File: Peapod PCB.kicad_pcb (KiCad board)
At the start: 2 copper layers, 70.9 x 27.2 mm, 20 parts, among them U1 ESP8266

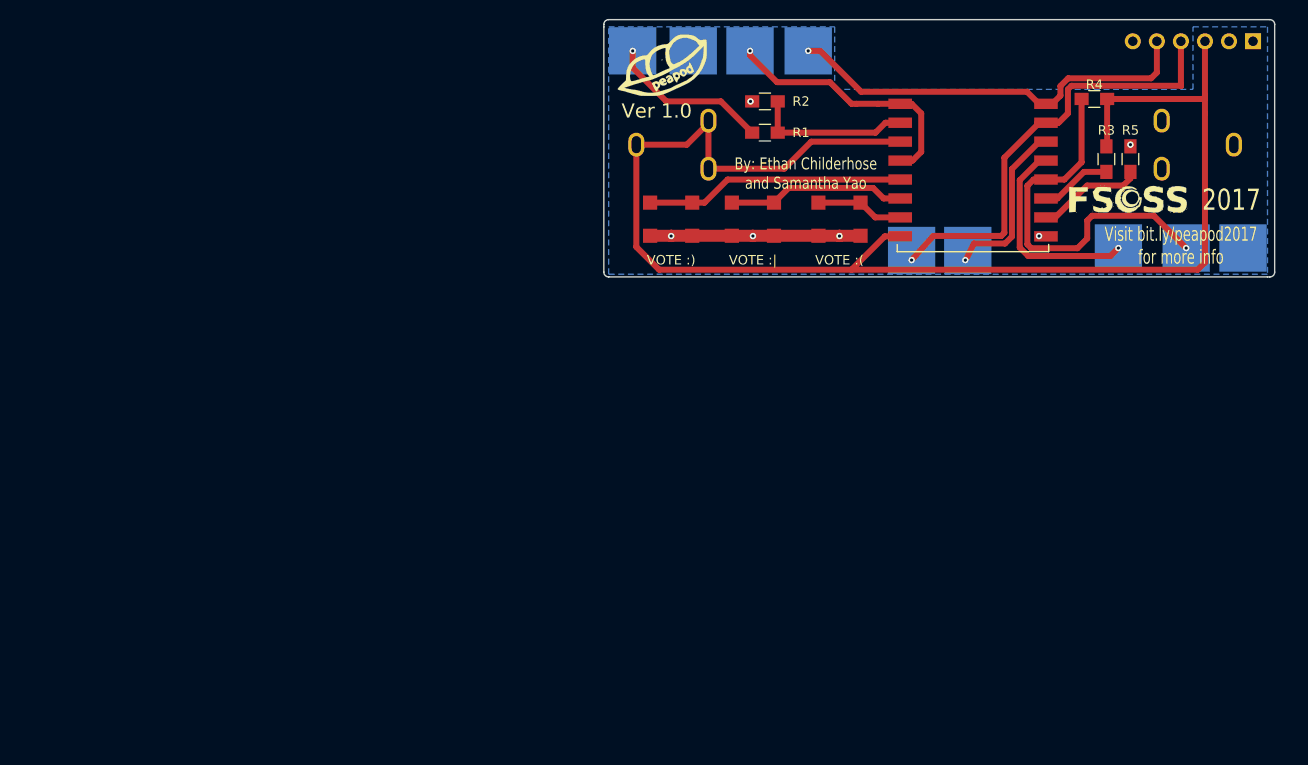
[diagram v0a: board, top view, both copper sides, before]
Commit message: initial plan for the outline of new peapod
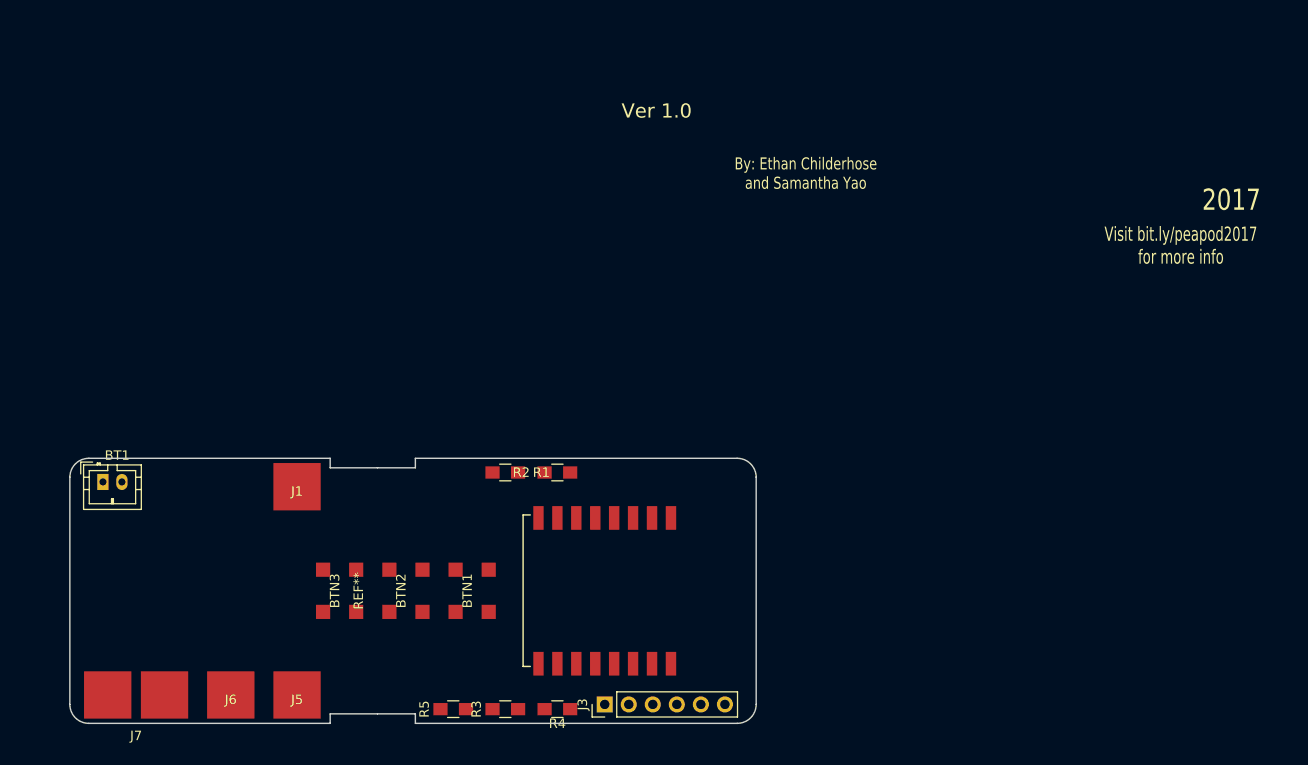
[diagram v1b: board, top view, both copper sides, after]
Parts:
- removed ANALOG, GPIO4, GPIO5, RX, TX: CONN_01X01, mod:Alligator Pad
- removed FTDI 3.3V: CONN_01X06, Pin_Headers:Pin_Header_Straight_1x06_Pitch2.54mm
- removed G***: LOGO, mod:LOGO
- removed G***: LOGO, mod:fsoss
- removed GND   GPIO0: CONN_01X02, mod:Bridge Pad
- removed RESET   GND: CONN_01X02, mod:Bridge Pad
- removed VOTE :(: Pushbutton, mod:Pushbutton
- removed VOTE :): Pushbutton, mod:Pushbutton
- removed VOTE :|: Pushbutton, mod:Pushbutton
- added BTN1: Pushbutton, mod:Pushbutton, F.Cu at (139.0, 86.5)
- added BTN2: Pushbutton, mod:Pushbutton, F.Cu at (132.0, 86.5)
- added BTN3: Pushbutton, mod:Pushbutton, F.Cu at (125.0, 86.5)
- added J1: CONN_01X01, mod:Alligator Pad, F.Cu at (120.5, 75.5)
- added J3: CONN_01X06, Pin_Headers:Pin_Header_Straight_1x06_Pitch2.54mm, F.Cu at (153.0, 98.5)
- added J5: CONN_01X01, mod:Alligator Pad, F.Cu at (120.5, 97.5)
- added J6: CONN_01X01, mod:Alligator Pad, F.Cu at (113.5, 97.5)
- added J7: CONN_01X02, mod:Bridge Pad, F.Cu at (103.5, 97.5)
- added REF**: 18650_outline, 18650_outline, F.Cu at (128.0, 86.5)
- BT1: footprint mod:BatteryMount -> Connectors_JST:JST_PH_B2B-PH-K_02x2.00mm_Straight
- moved BT1 94.9 mm to (100.0, 75.0), turned to 0 degrees
- moved R5 92.2 mm to (137.0, 99.0), turned to 180 degrees
- moved R3 86.1 mm to (142.5, 99.0), turned to 0 degrees
- moved R4 85.9 mm to (148.0, 99.0), turned to 180 degrees
- moved U1 51.0 mm to (160.0, 79.5), turned to 270 degrees
- moved R1 45.2 mm to (142.5, 74.0)
- moved R2 44.9 mm to (148.0, 74.0), turned to 0 degrees
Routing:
- net +3V3: track 154.5 -> 0.00 mm
- net Net-(J3-Pad4): track 47.5 -> 0.00 mm, vias 1 -> 0
- net Net-(J3-Pad5): track 46.3 -> 0.00 mm, vias 1 -> 0
- net Net-(J7-Pad1): track 40.5 -> 0.00 mm, vias 1 -> 0
- net Net-(BTN2-Pad2): track 28.1 -> 0.00 mm
- net Net-(J2-Pad1): track 27.1 -> 0.00 mm, vias 1 -> 0
- net GND: track 22.3 -> 0.00 mm, vias 6 -> 0
- net Net-(J6-Pad1): track 21.2 -> 0.00 mm, vias 1 -> 0
- net Net-(BTN1-Pad2): track 19.6 -> 0.00 mm
- net Net-(R1-Pad1): track 17.4 -> 0.00 mm
- net Net-(J1-Pad1): track 17.2 -> 0.00 mm, vias 1 -> 0
- net Net-(J5-Pad1): track 17.2 -> 0.00 mm, vias 1 -> 0
- net Net-(R5-Pad1): track 12.0 -> 0.00 mm
- net Net-(BTN3-Pad2): track 9.98 -> 0.00 mm
- net Net-(R3-Pad2): track 8.25 -> 0.00 mm
- removed copper zone on B.Cu, net GND
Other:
- board size 70.9 x 27.2 mm -> 72.5 x 28 mm

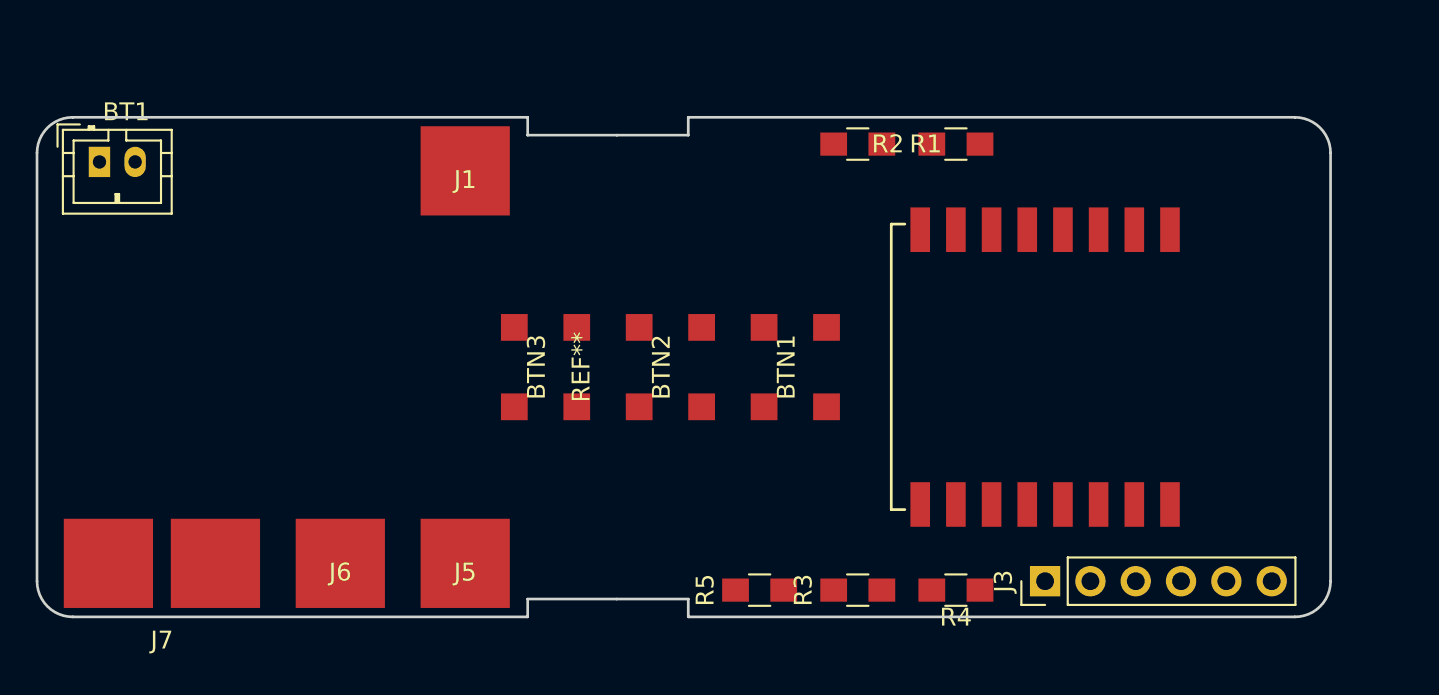
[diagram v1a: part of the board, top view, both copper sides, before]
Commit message: new peapod with routing complete
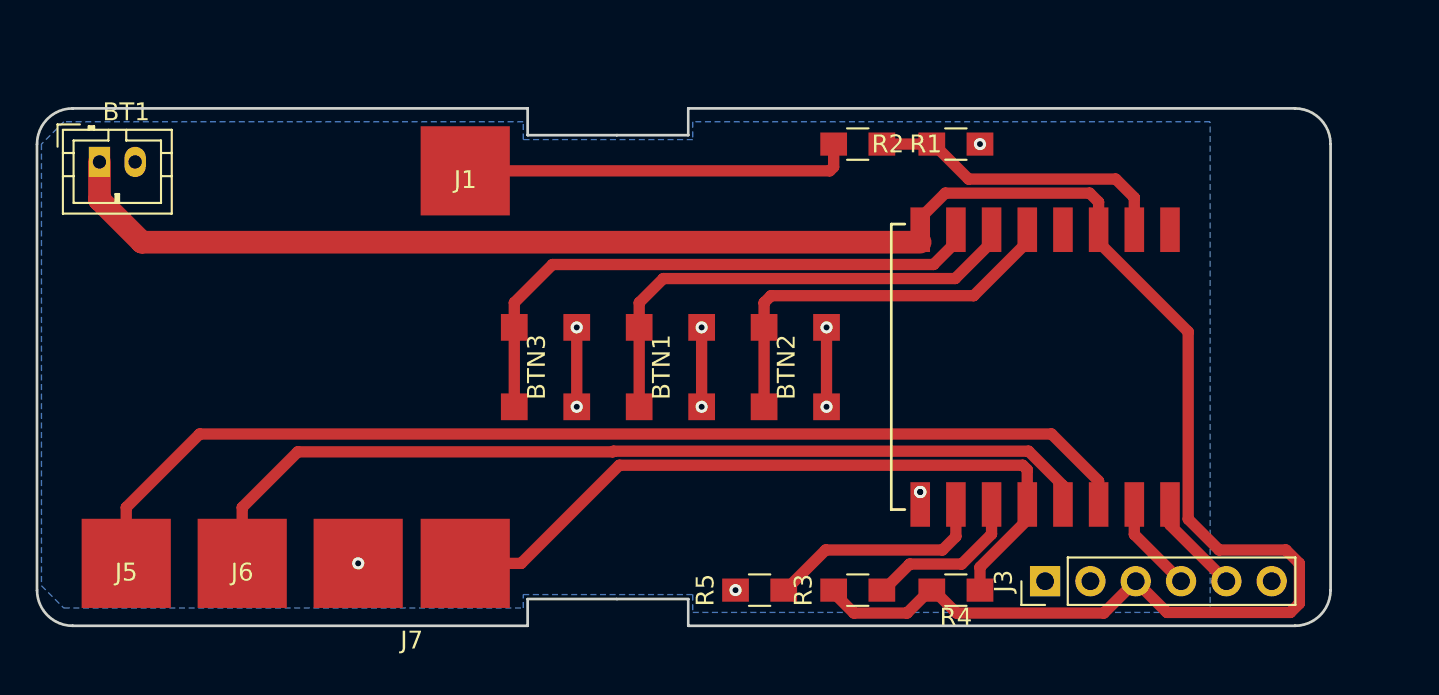
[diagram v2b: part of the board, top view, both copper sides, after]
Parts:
- moved J5 19.0 mm to (101.5, 97.5)
- moved J7 14.0 mm to (117.5, 97.5)
- moved BTN1 7.00 mm to (132.0, 86.5)
- moved BTN2 7.00 mm to (139.0, 86.5)
- moved J6 5.50 mm to (108.0, 97.5)
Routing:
- net +3V3: track 0.00 -> 120.1 mm
- net Net-(J5-Pad1): track 0.00 -> 61.0 mm
- net Net-(J6-Pad1): track 0.00 -> 51.6 mm
- net Net-(J7-Pad1): track 0.00 -> 41.7 mm
- net Net-(BTN3-Pad2): track 0.00 -> 32.0 mm
- net Net-(BTN1-Pad2): track 0.00 -> 27.0 mm
- net Net-(J1-Pad1): track 0.00 -> 22.0 mm
- net Net-(BTN2-Pad2): track 0.00 -> 22.0 mm
- net Net-(R1-Pad1): track 0.00 -> 17.9 mm
- net Net-(R5-Pad1): track 0.00 -> 13.4 mm
- net GND: track 0.00 -> 13.3 mm, vias 0 -> 11
- net Net-(R3-Pad2): track 0.00 -> 9.81 mm
- net Net-(J3-Pad5): track 0.00 -> 6.31 mm
- net Net-(J3-Pad4): track 0.00 -> 6.09 mm
- added copper zone on B.Cu, net GND
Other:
- board size 72.5 x 28 mm -> 72.5 x 29 mm

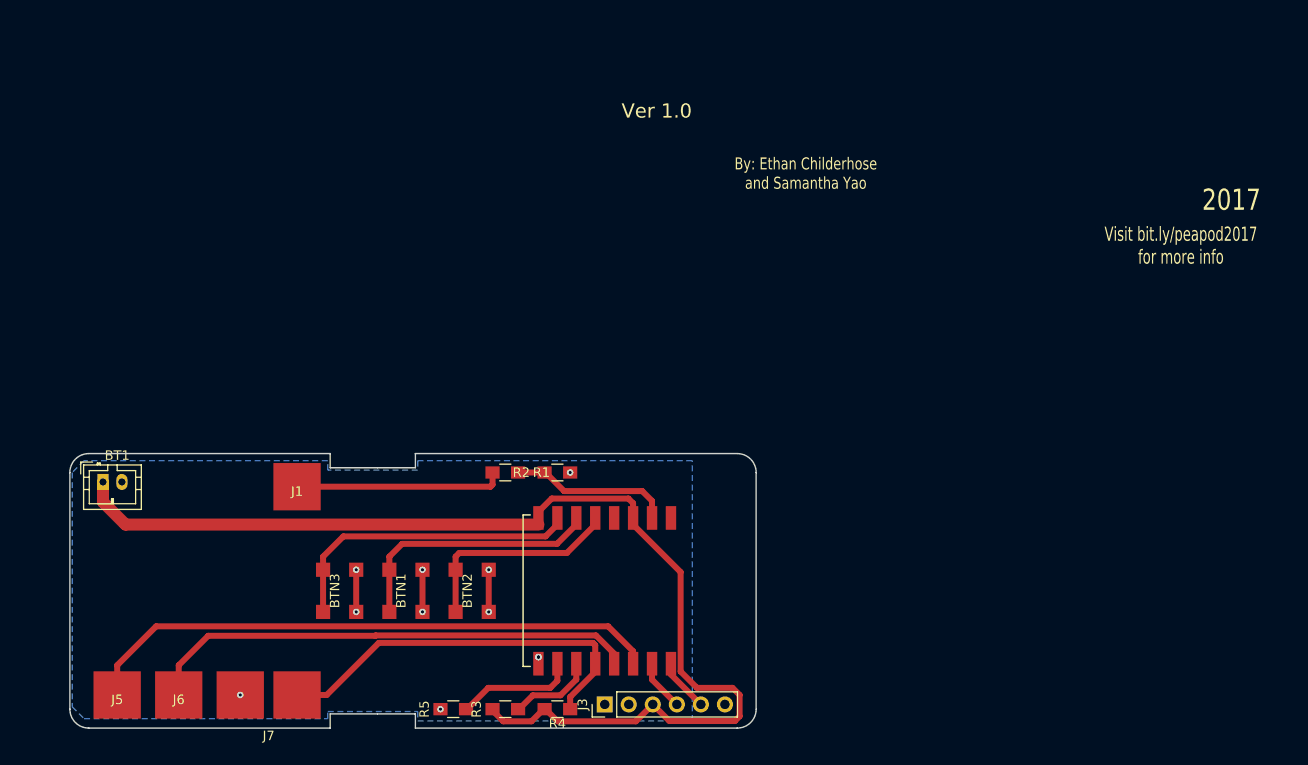
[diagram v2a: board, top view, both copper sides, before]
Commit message: routing done, silkscreen in progress
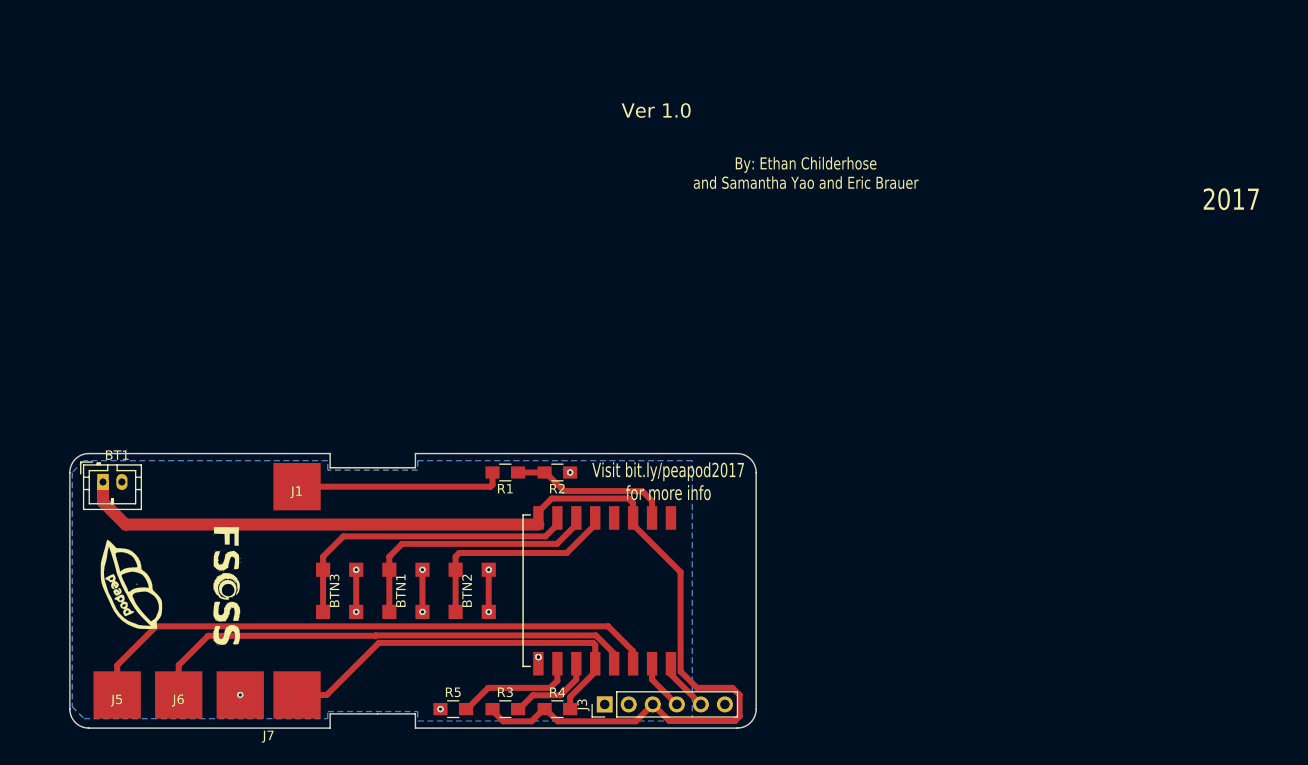
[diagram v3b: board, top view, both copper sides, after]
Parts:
- added G***: LOGO, mod:peapod, F.Cu at (102.8, 86.0)
- added G***: LOGO, mod:fsoss, F.Cu at (112.8, 86.5)
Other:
- board text added: "By: Ethan Childerhose and Samantha Yao and Eric Brauer"
- board text removed: "By: Ethan Childerhose and Samantha Yao"

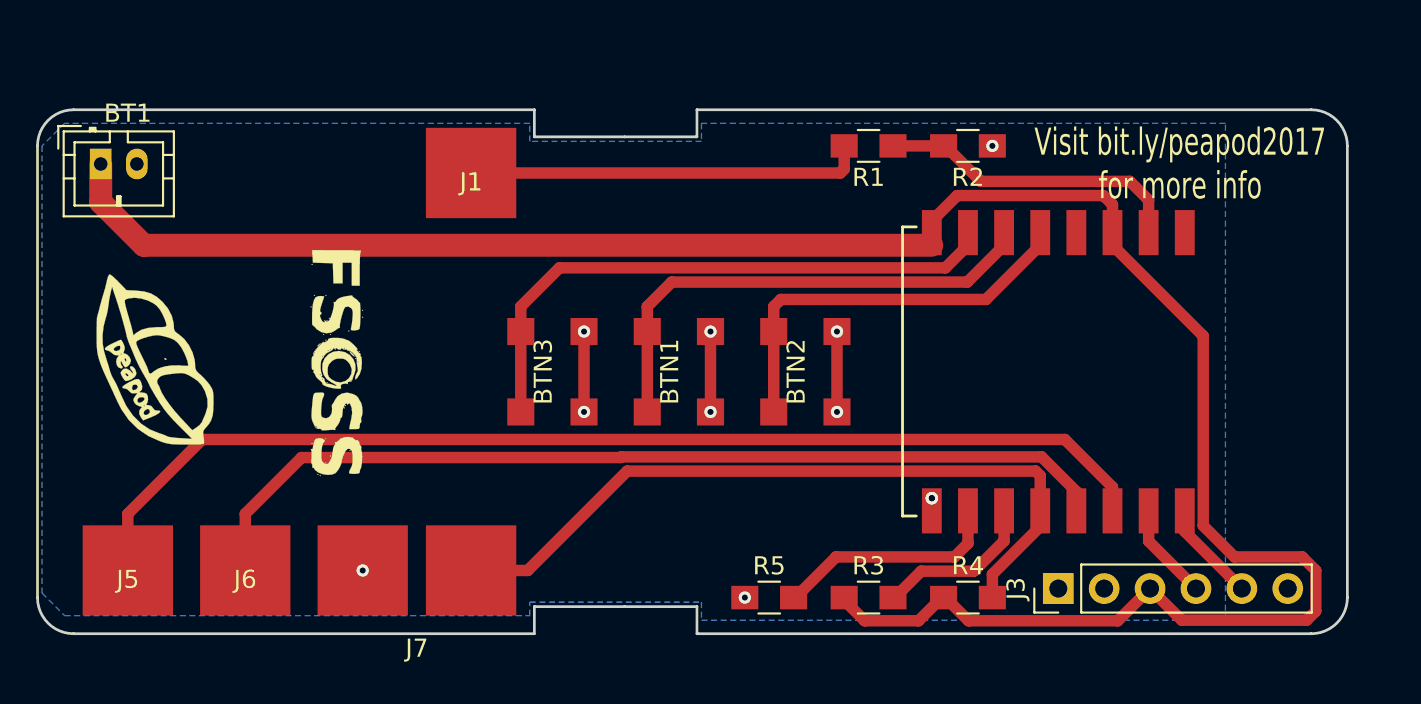
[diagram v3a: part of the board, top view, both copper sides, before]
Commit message: fixed a problem with previous shape
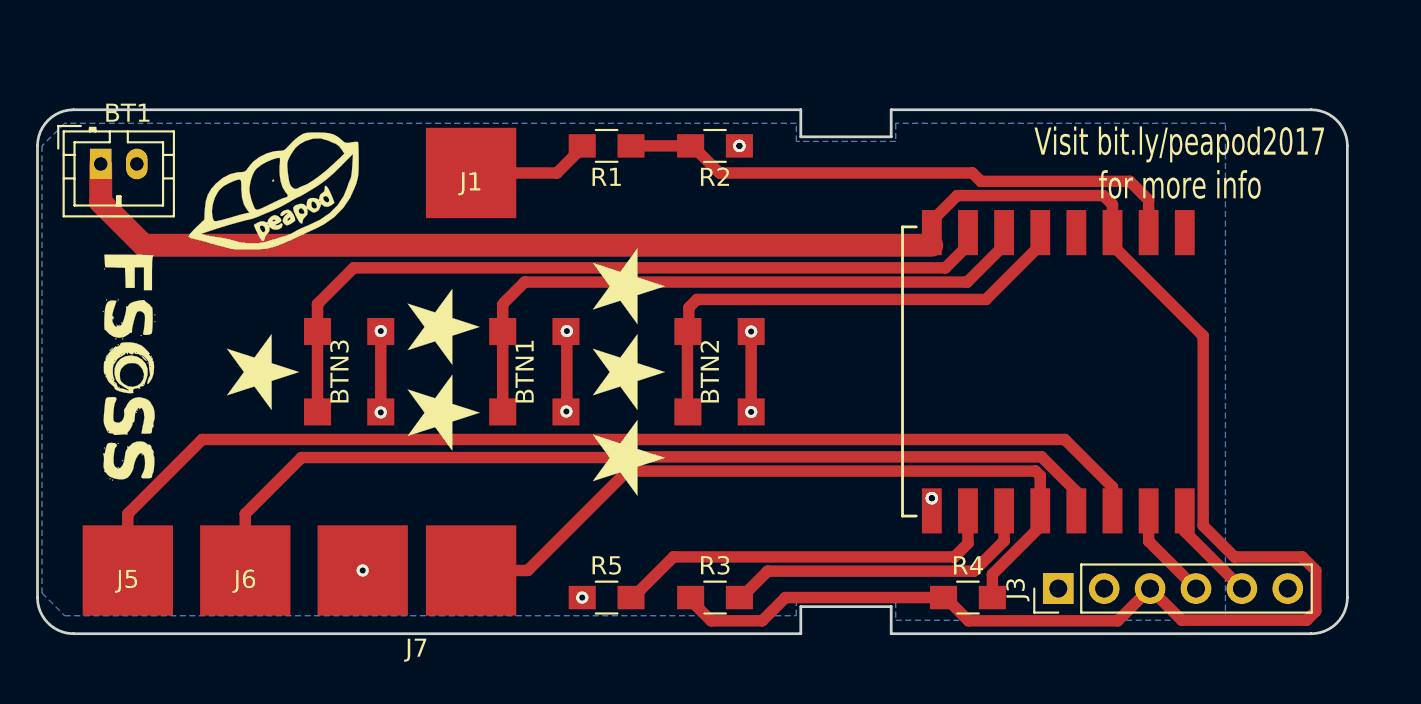
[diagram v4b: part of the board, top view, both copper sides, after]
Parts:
- added G***: LOGO, LOGO, F.Cu at (129.2, 91.2)
- added G***: LOGO, LOGO, F.Cu at (129.2, 86.5)
- added G***: LOGO, LOGO, F.Cu at (129.2, 81.8)
- added G***: LOGO, LOGO, F.Cu at (119.0, 88.8)
- added G***: LOGO, LOGO, F.Cu at (119.0, 84.0)
- added G***: LOGO, LOGO, F.Cu at (109.0, 86.5)
- moved R1 14.5 mm to (128.0, 74.0)
- moved R2 14.0 mm to (134.0, 74.0)
- moved G*** 11.6 mm to (109.8, 76.8), turned to 0 degrees
- moved G*** 11.5 mm to (101.2, 86.8)
- moved BTN3 11.2 mm to (113.8, 86.5)
- moved R5 9.00 mm to (128.0, 99.0)
- moved R3 8.50 mm to (134.0, 99.0)
- moved BTN1 8.00 mm to (124.0, 86.5)
- moved BTN2 4.75 mm to (134.2, 86.5)
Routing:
- net Net-(J1-Pad1): track 22.0 -> 6.87 mm
- net Net-(R1-Pad1): track 17.9 -> 32.4 mm
- net Net-(BTN3-Pad2): track 32.0 -> 43.4 mm
- net Net-(R5-Pad1): track 13.4 -> 22.4 mm
- net +3V3: track 120.1 -> 128.7 mm
- net Net-(R3-Pad2): track 9.81 -> 18.3 mm
- net Net-(BTN1-Pad2): track 27.0 -> 34.9 mm
- net Net-(BTN2-Pad2): track 22.0 -> 26.7 mm
- net GND: track 13.3 -> 13.4 mm, vias 11 -> 12
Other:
- outline, holes or cut-outs redrawn

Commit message: silkscreening done. Pending approval.
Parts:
- BT1: moved to B.Cu
- moved BT1 2.93 mm to (102.8, 74.0), turned to 180 degrees
- moved G*** 2.00 mm to (101.2, 84.8)
- moved G*** 0.50 mm to (109.8, 77.2), turned to 270 degrees
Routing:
- net +3V3: track 128.7 -> 125.1 mm
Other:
- board text added: "ADC"
- board text added: "ANALOG 3.3v to 1v: R2 = 10k, R1 = 25k"
- board text added: "GPIO0"
- board text added: "GPIO4"
- board text added: "GPIO5"
- board text added: "Ver 1.1"
- board text removed: "ANALOG 3.3v to 1v R2 = 10k R1 = 25k"
- board text removed: "Ver 1.0"
